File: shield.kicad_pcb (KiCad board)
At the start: 4 copper layers, 150 x 120 mm, 158 parts, among them J1 NAPPE_ADC1, J10 OLED_SPI_2x8, J13 NAPPE_LOGIC, J14 NAPPE_COM, J2 NAPPE_ADC2, J3 NAPPE_PWM, J4 NAPPE_GPIO1, J5 DEVKIT_C2000_ROW_A, J6 DEVKIT_C2000_ROW_B, J7 ESP32_C6_DEVKITC_1_J1, J8 ESP32_C6_DEVKITC_1_J3, J9 J_PWR_11-25V, U1 LDO_3V3_ISO, U2 NCM3S1205MC, U3 NCM3S1205MC, U4 ER-OLEDM032-1

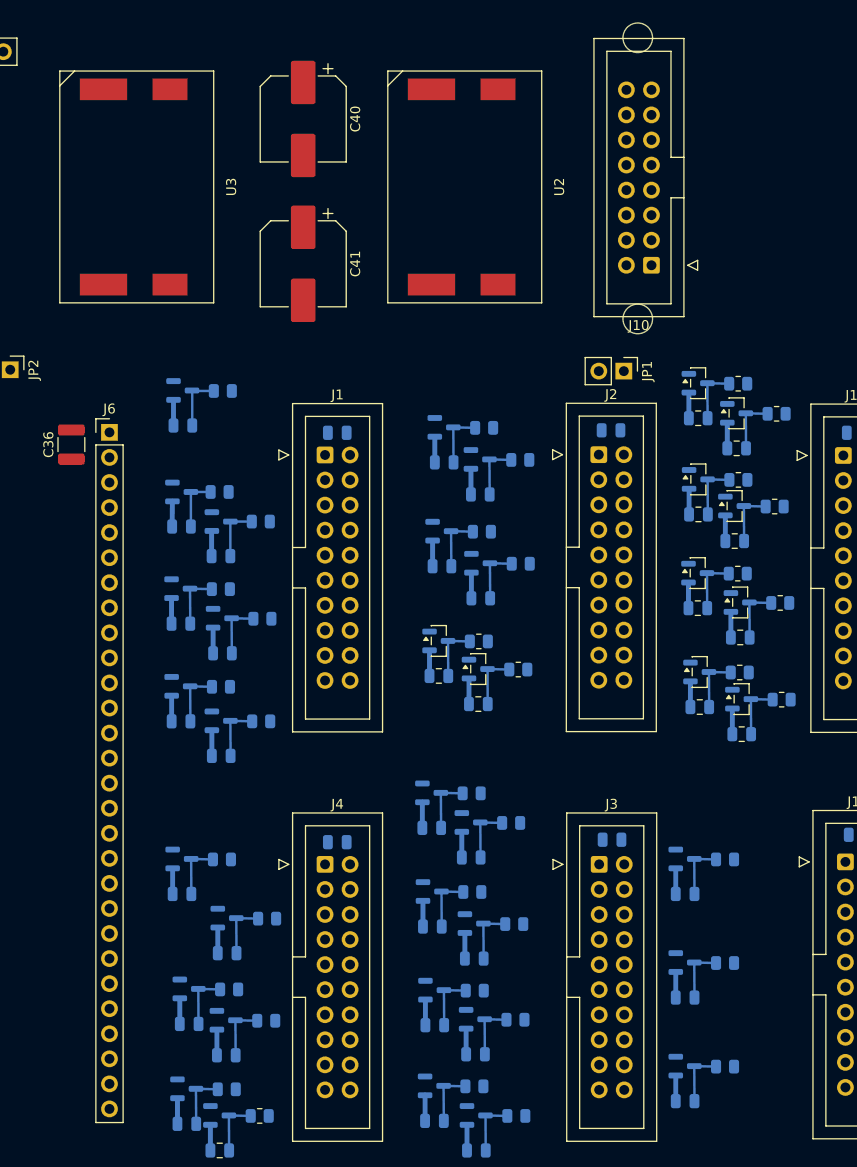
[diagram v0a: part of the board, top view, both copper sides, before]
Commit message: NCM3S1205MC : empreinte et symbole remplaces par le modele telecharge SnapEDA (decision #21)
Footprint (lib/NCM3S1205MC.kicad_mod + copies U2/U3 dans shield.kicad_pcb)
repris du modele SnapEDA CONV_NCM3S1205MC-R7 (pastilles a +/-11.0mm),
cotes confirmees par l'utilisateur contre la page 10 du datasheet Murata -
l'ancien footprint fait main (decision #15) est remplace, pas seulement
complete. Noms de broches repris cote symbole (-VIN/+VIN/+VOUT/-VOUT),
position/longueur/type electrique inchanges pour ne pas desaligner les
fils reels de dc.kicad_sch ni casser le role de driver implicite de
+VOUT sur le net GND (verifie par ERC/DRC, categories identiques avant/apres).

Co-Authored-By: Claude Sonnet 5 <noreply@anthropic.com>
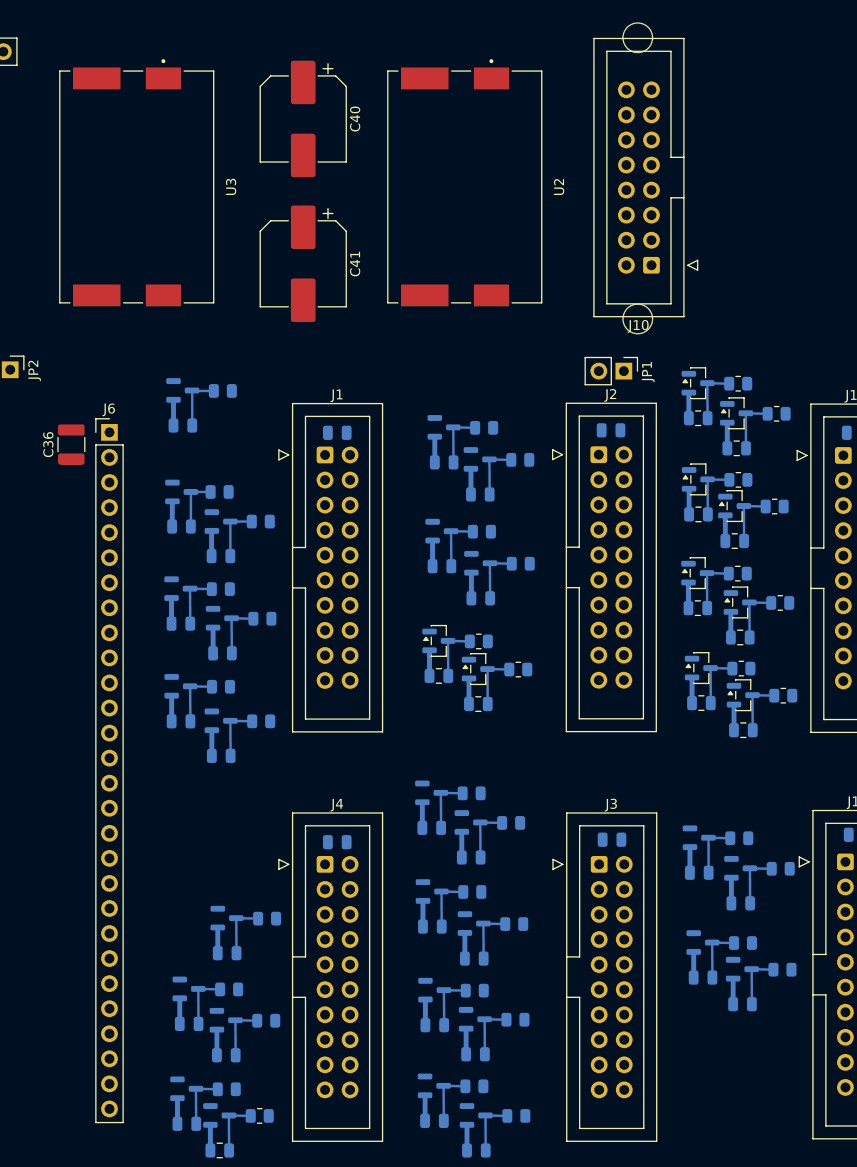
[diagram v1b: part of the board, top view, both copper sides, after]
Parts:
- moved D36 52.5 mm to (235.6, 119.0)
- moved C55 52.5 mm to (235.7, 122.6)
- moved R35 52.5 mm to (239.7, 119.1)
- moved D39 11.4 mm to (240.0, 132.4)
- moved R38 11.4 mm to (244.1, 132.4)
- moved C58 11.4 mm to (240.0, 135.9)
- moved D37 5.72 mm to (239.8, 122.2)
- moved R36 5.72 mm to (243.9, 122.2)
- moved C56 5.72 mm to (239.9, 125.7)
- moved R37 2.72 mm to (240.1, 129.7)
- moved C57 2.72 mm to (236.0, 133.2)
- moved D38 2.72 mm to (236.0, 129.7)
- moved D34 0.43 mm to (240.1, 104.6)
- moved D35 0.43 mm to (235.9, 101.8)
- moved C53 0.43 mm to (240.1, 108.2)
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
